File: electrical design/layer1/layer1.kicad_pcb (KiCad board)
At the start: 2 copper layers, 178 x 168.1 mm, 204 parts, among them J2 1x07 2.54 FEMALE, J3 1x07 2.54 FEMALE, J4 XT30PW-F, Q1 MOSFET-NCH-FQP30N06L, Q2 MOSFET-NCH-AO3404A, SW1 SW_DPDT_x2, U1 CD74HC4067SM, U2 CD74HC4067SM

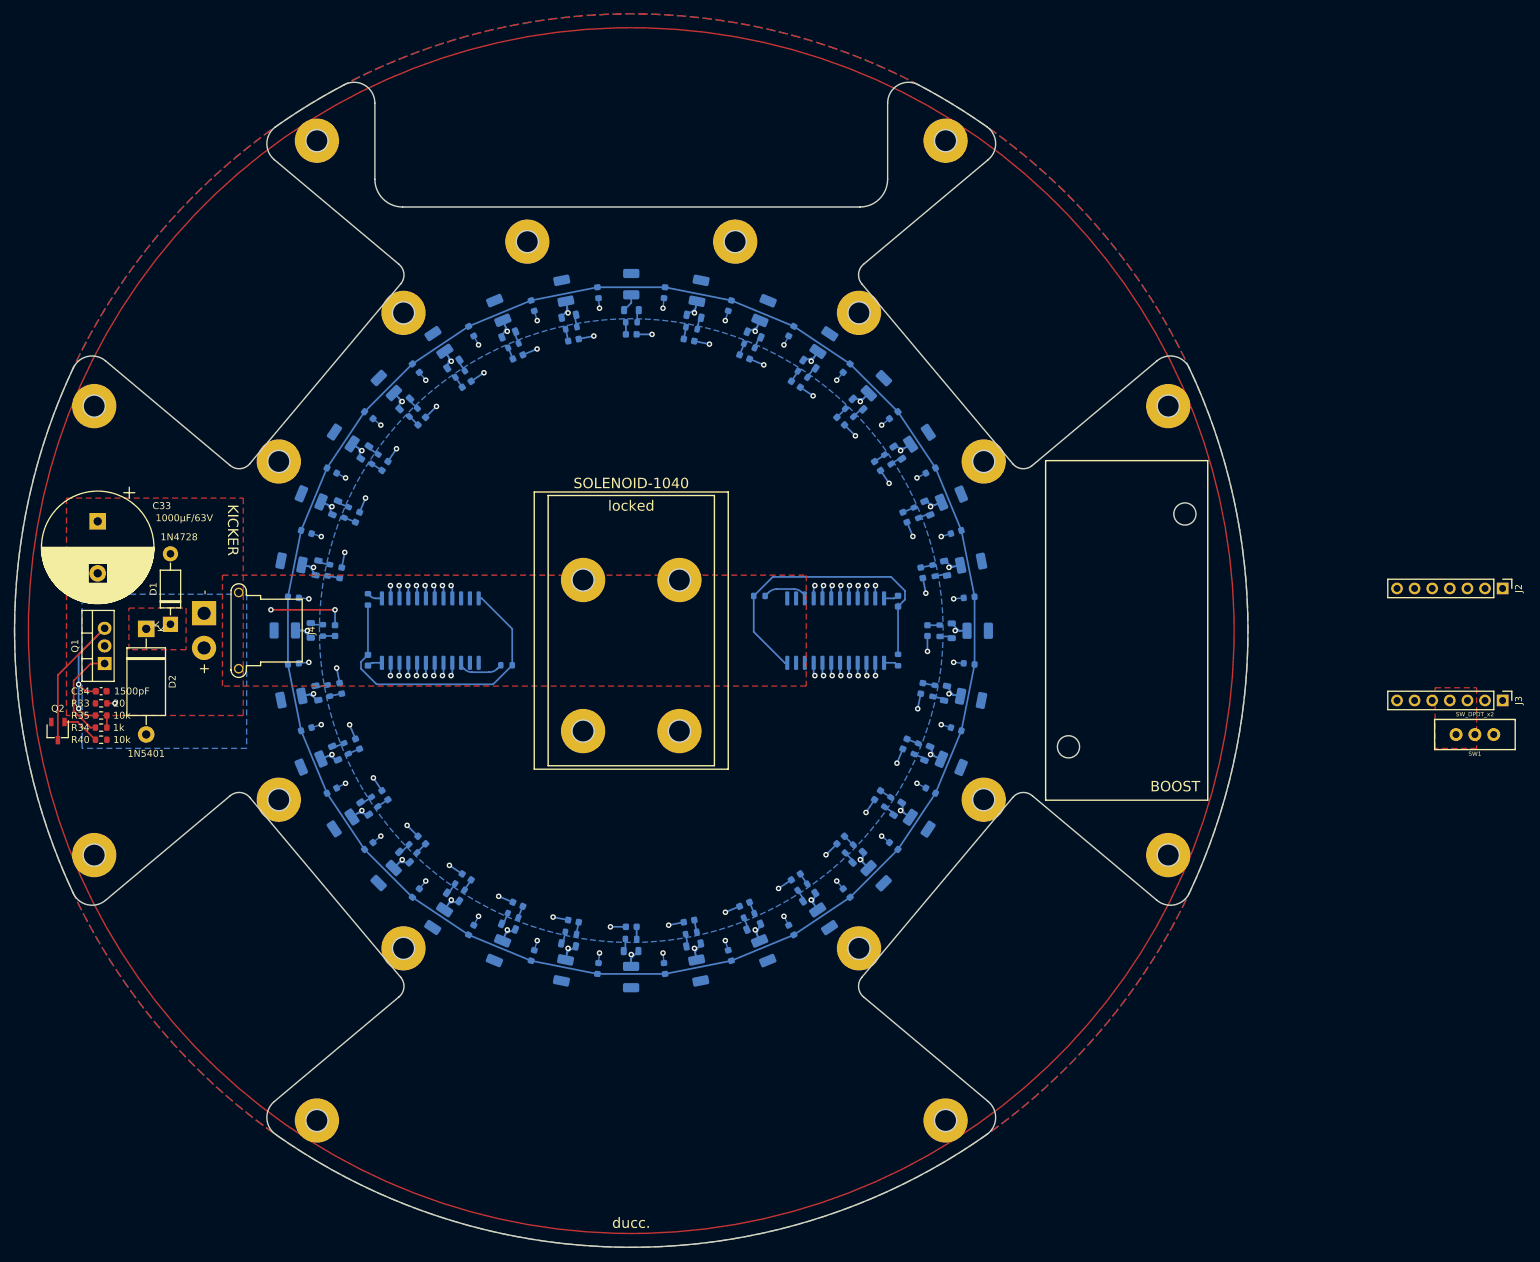
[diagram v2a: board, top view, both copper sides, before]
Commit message: add boost to l1 pcb and update mech drawing
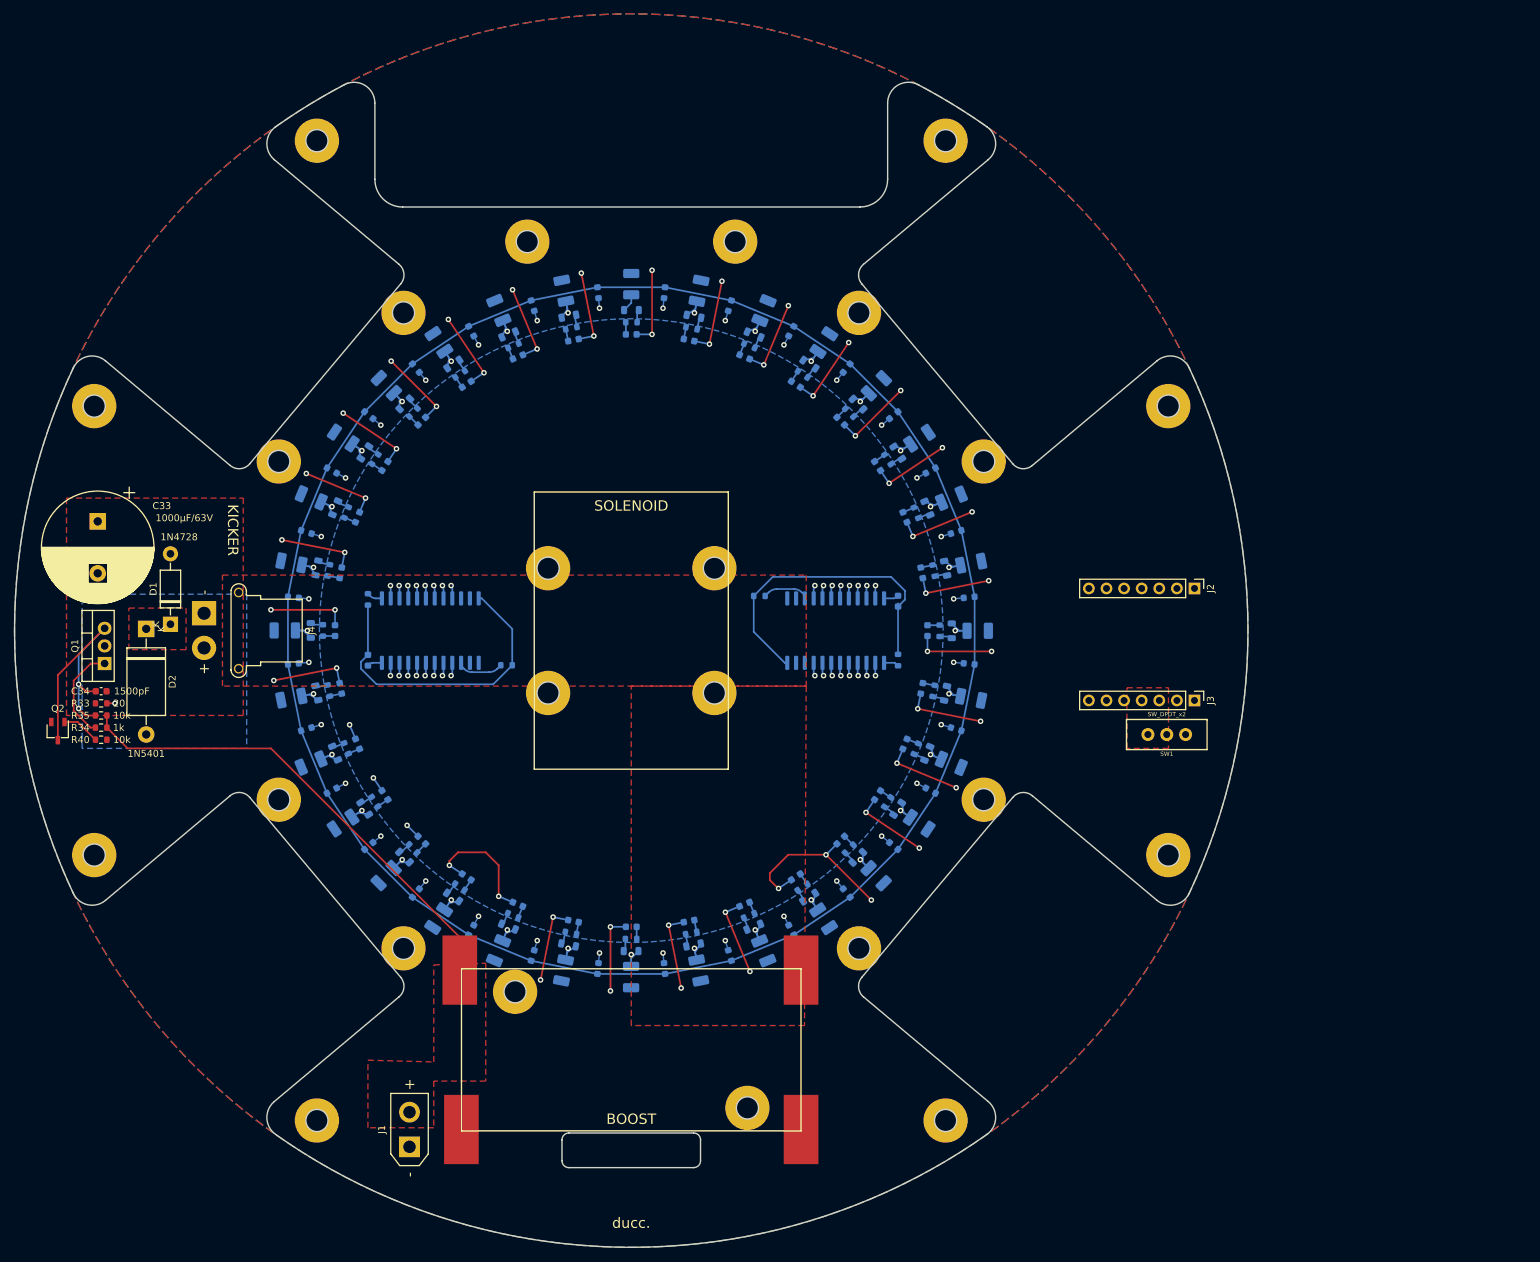
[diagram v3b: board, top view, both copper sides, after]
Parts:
- added H23: MountingHole, MountingHole:MountingHole_3.2mm_M3_Pad, F.Cu at (88.2, 157.1)
- added H24: MountingHole, MountingHole:MountingHole_3.2mm_M3_Pad, F.Cu at (121.8, 173.9)
- added J1: XT60-F, Connector_AMASS:AMASS_XT30UPB-F_1x02_P5.0mm_Vertical, F.Cu at (73.0, 179.5)
- added J5: Conn_01x01_Socket, Connector_Wire:SolderWirePad_1x01_SMD_5x10mm, F.Cu at (80.2, 154.0)
- added J6: Conn_01x01_Socket, Connector_Wire:SolderWirePad_1x01_SMD_5x10mm, F.Cu at (80.5, 177.0)
- added J7: Conn_01x01_Socket, Connector_Wire:SolderWirePad_1x01_SMD_5x10mm, F.Cu at (129.5, 154.0)
- added J8: Conn_01x01_Socket, Connector_Wire:SolderWirePad_1x01_SMD_5x10mm, F.Cu at (129.5, 177.0)
- moved J2 44.5 mm to (186.3, 98.9)
- moved J3 44.5 mm to (186.3, 115.1)
- moved SW1 44.5 mm to (182.3, 120.0)
- moved H12 7.47 mm to (117.0, 114.0)
- moved H17 7.47 mm to (93.0, 114.0)
- moved H7 5.33 mm to (117.0, 96.0)
- moved H8 5.33 mm to (93.0, 96.0)
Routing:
- net GND: track 80.5 -> 337.2 mm, vias 33 -> 58
- net +12V: track 1.75 -> 70.0 mm
- added copper zone on F.Cu, net +12V
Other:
- outline, holes or cut-outs redrawn
- board text added: "SOLENOID"
- board text removed: "SOLENOID-1040"
- board text removed: "locked"

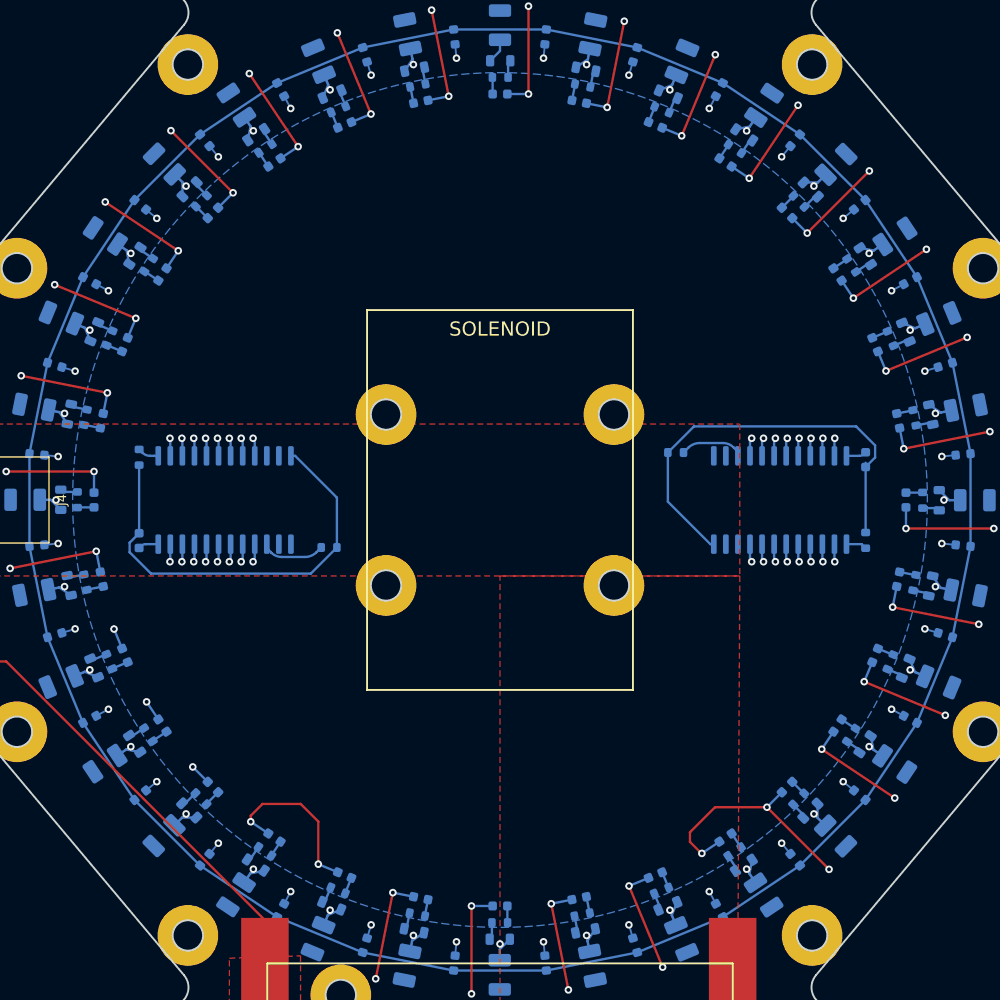
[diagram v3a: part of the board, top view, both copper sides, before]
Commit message: routed l1 mux
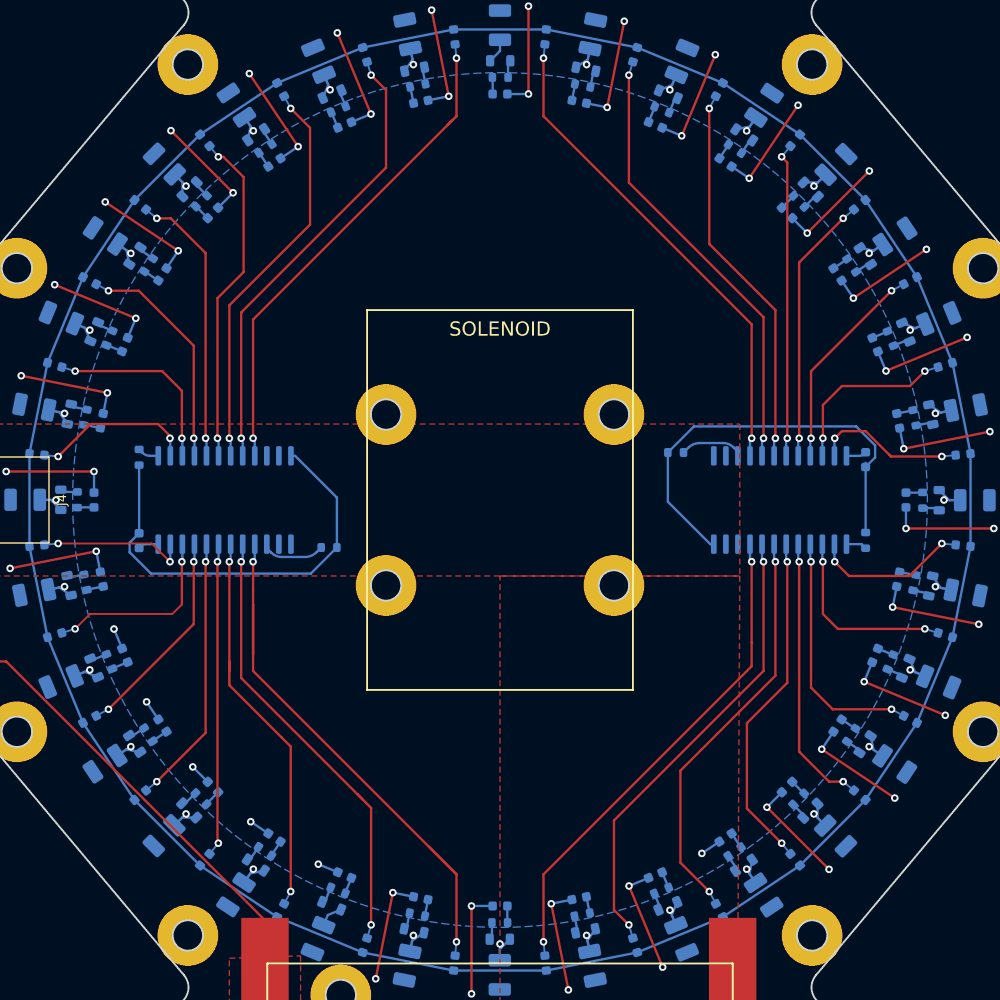
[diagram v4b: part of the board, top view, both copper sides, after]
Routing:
- net Net-(U1-I15): track 3.38 -> 61.7 mm
- net Net-(U1-I0): track 3.42 -> 53.6 mm
- net Net-(U2-I15): track 3.38 -> 52.5 mm
- net Net-(U2-I0): track 3.38 -> 52.5 mm
- net Net-(U1-I14): track 3.38 -> 49.3 mm
- net Net-(U2-I1): track 3.38 -> 48.8 mm
- net Net-(U1-I1): track 3.38 -> 48.6 mm
- net Net-(U2-I14): track 3.38 -> 47.5 mm
- net Net-(U2-I2): track 3.37 -> 43.5 mm
- net Net-(U1-I13): track 3.37 -> 43.3 mm
- net Net-(U1-I2): track 3.37 -> 42.5 mm
- net Net-(U2-I13): track 3.37 -> 41.0 mm
- net Net-(U2-I3): track 3.36 -> 36.3 mm
- net Net-(U1-I3): track 3.36 -> 35.5 mm
- net Net-(U2-I12): track 3.36 -> 33.2 mm
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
